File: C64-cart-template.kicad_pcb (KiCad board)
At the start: 2 copper layers, 57.9 x 47.9 mm, 2 parts, among them J1 EXPANSION_PORT_C64

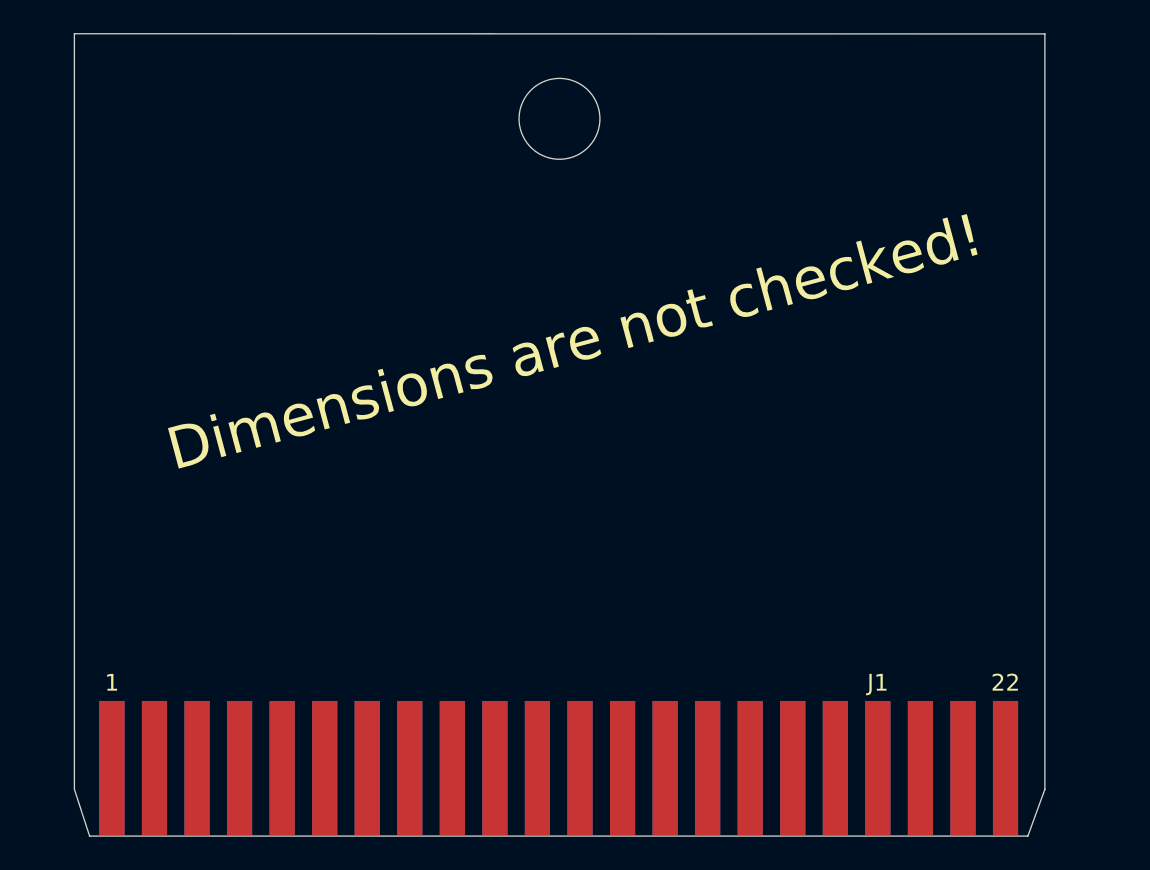
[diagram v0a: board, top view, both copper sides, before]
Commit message: fixed missing opening in solder mask on the bottom side.
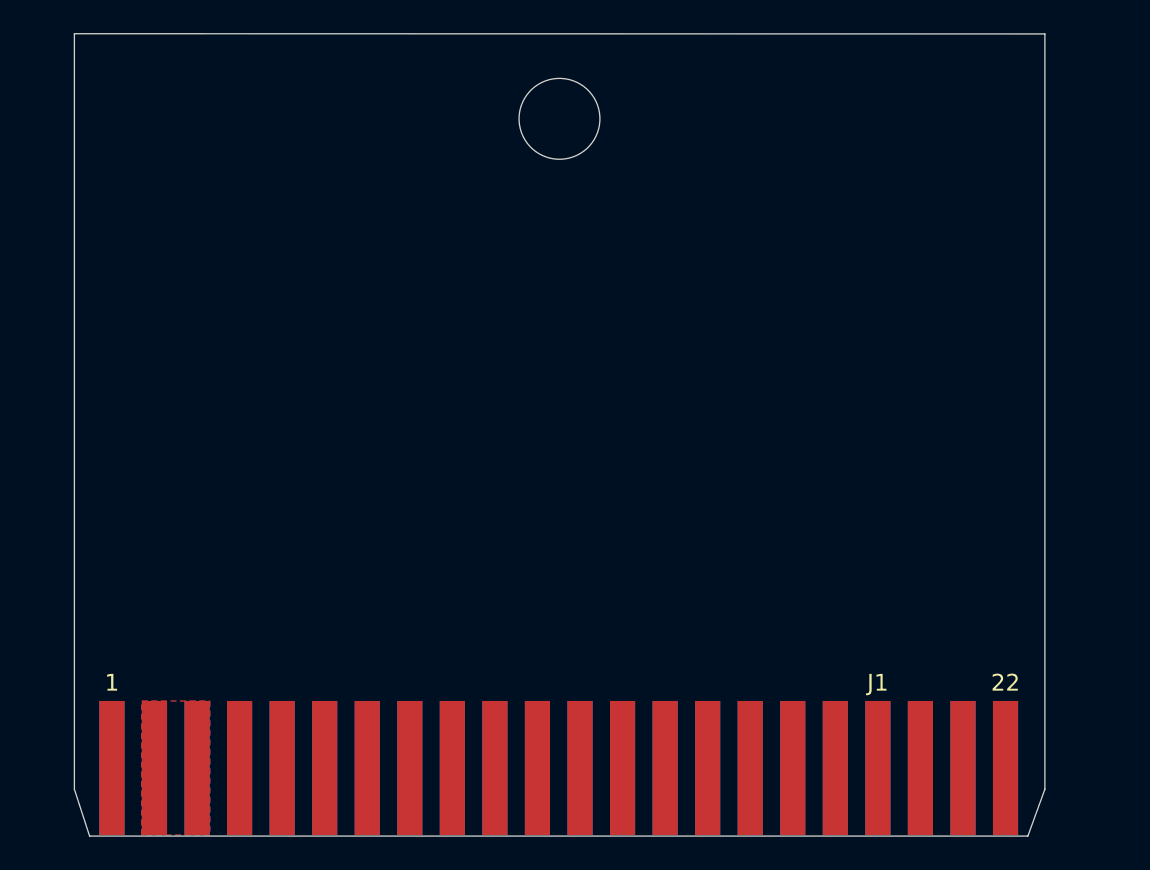
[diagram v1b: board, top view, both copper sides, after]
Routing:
- added copper zone on F.Cu, net +5V
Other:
- board text removed: "Dimensions are not checked!"
